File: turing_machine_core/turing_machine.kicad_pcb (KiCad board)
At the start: 2 copper layers, 165.1 x 110.5 mm, 57 parts, among them J1 External Interface, U1 74LS04, U10 AS6C1008, U11 74LS193, U12 74LS374, U13 74LS74, U14 74LS245, U15 74LS245, U16 74LS245, U17 74LS245, U18 74LS245, U19 74LS138, U2 74LS00, U20 74LS156, U3 AS6C1008, U4 74LS374, U5 74LS193, U6 74LS30, U7 AS6C1008, U8 74LS193, U9 74LS193

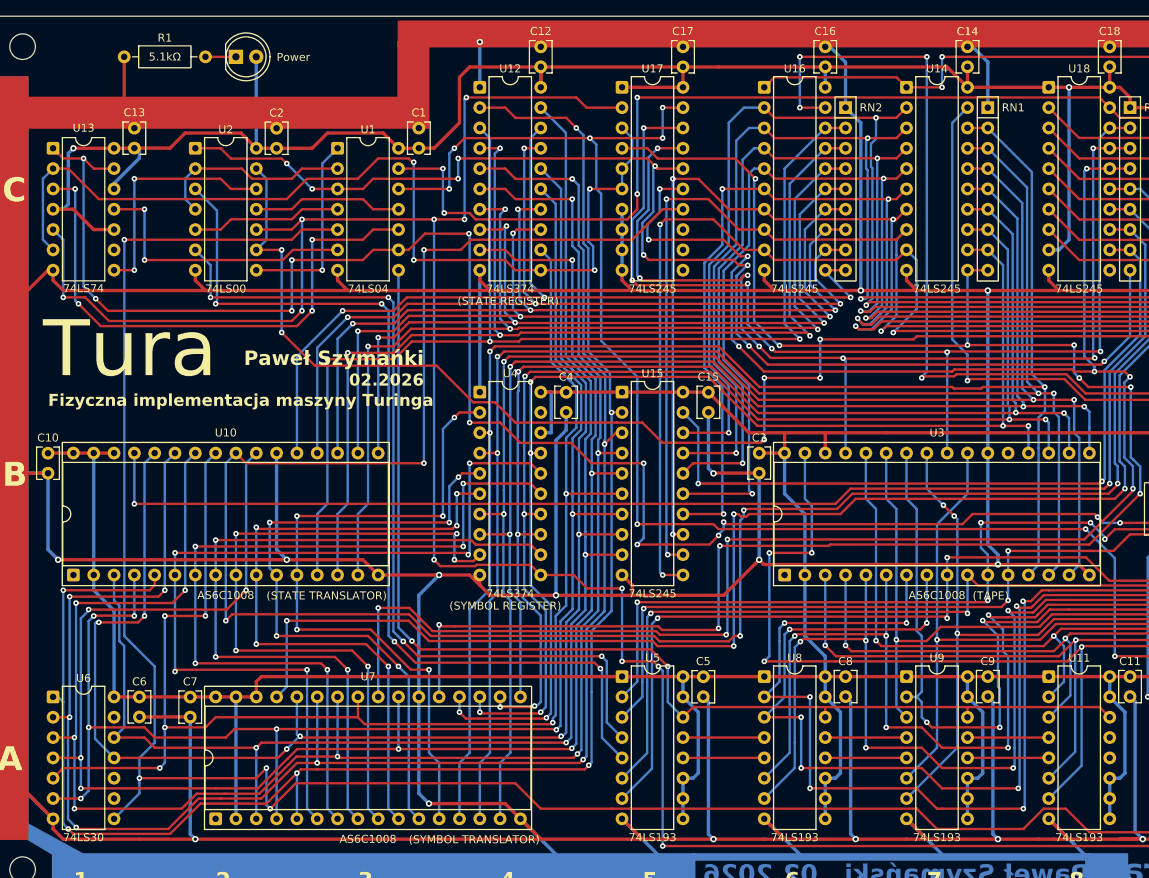
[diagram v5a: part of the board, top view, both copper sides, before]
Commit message: small cosmetic PCB changes
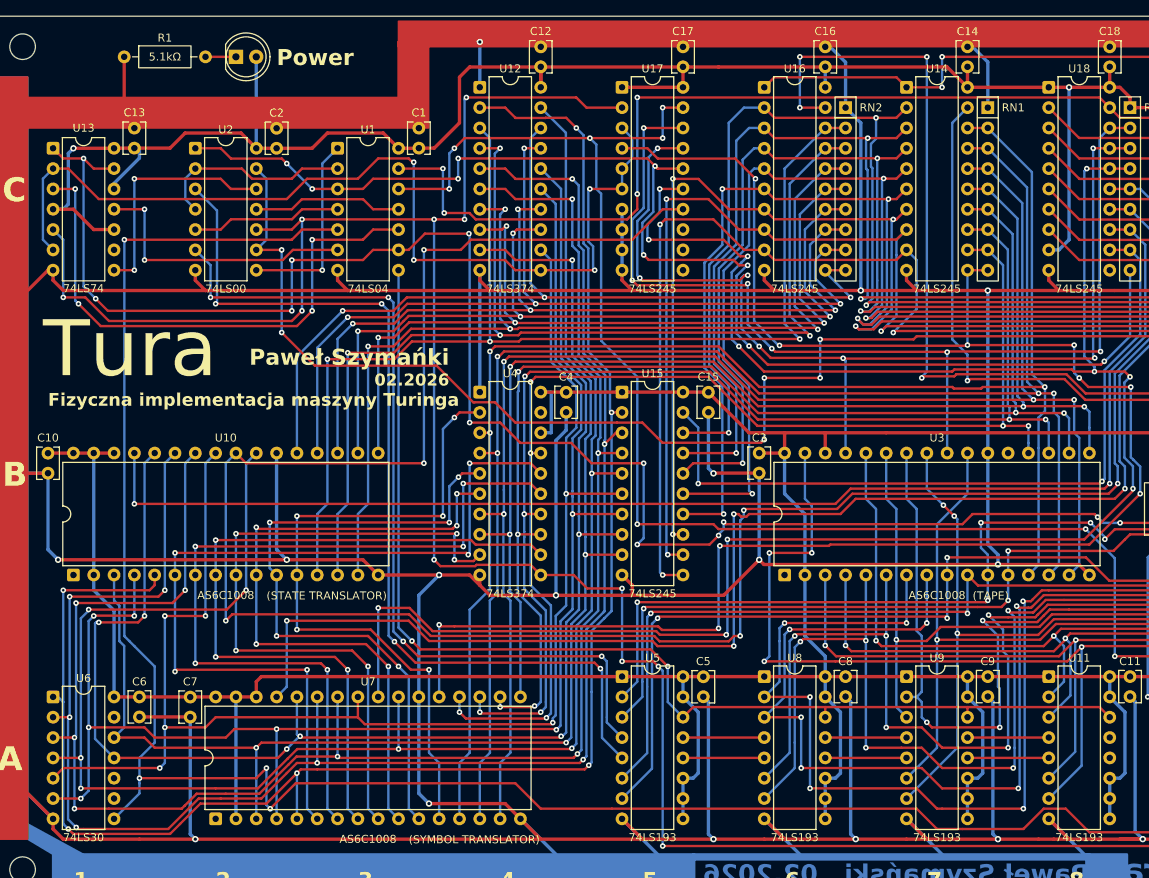
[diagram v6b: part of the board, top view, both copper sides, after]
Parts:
- removed the REF** at (226.1, 45.1)
- removed the REF** at (226.1, 64.1)
- U10, U3, U7: footprint Package_DIP:DIP-32_W15.24mm_Socket -> Package_DIP:DIP-32_W15.24mm
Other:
- board text removed: "(STATE REGISTER)"
- board text removed: "(SYMBOL REGISTER)"

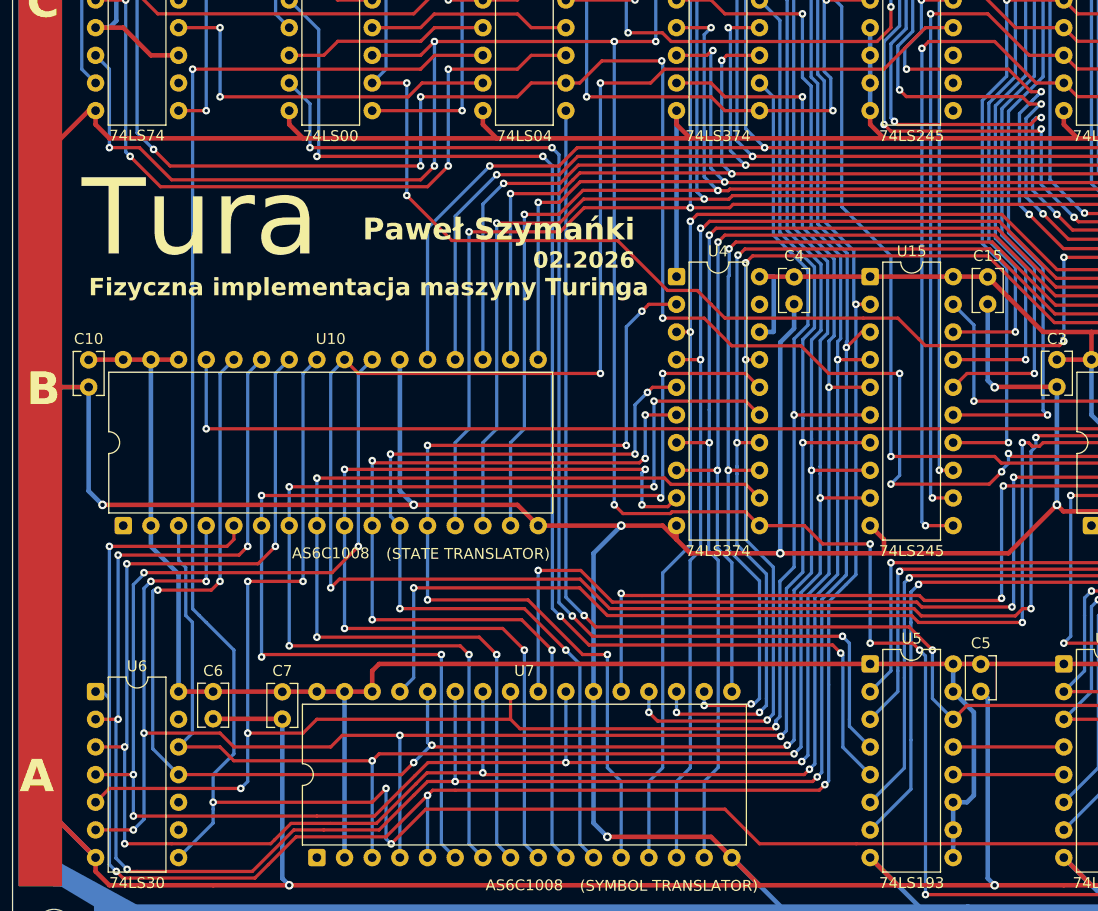
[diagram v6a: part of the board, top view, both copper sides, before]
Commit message: added two connectors to schematics and PCB design and reformatted slightly documentation
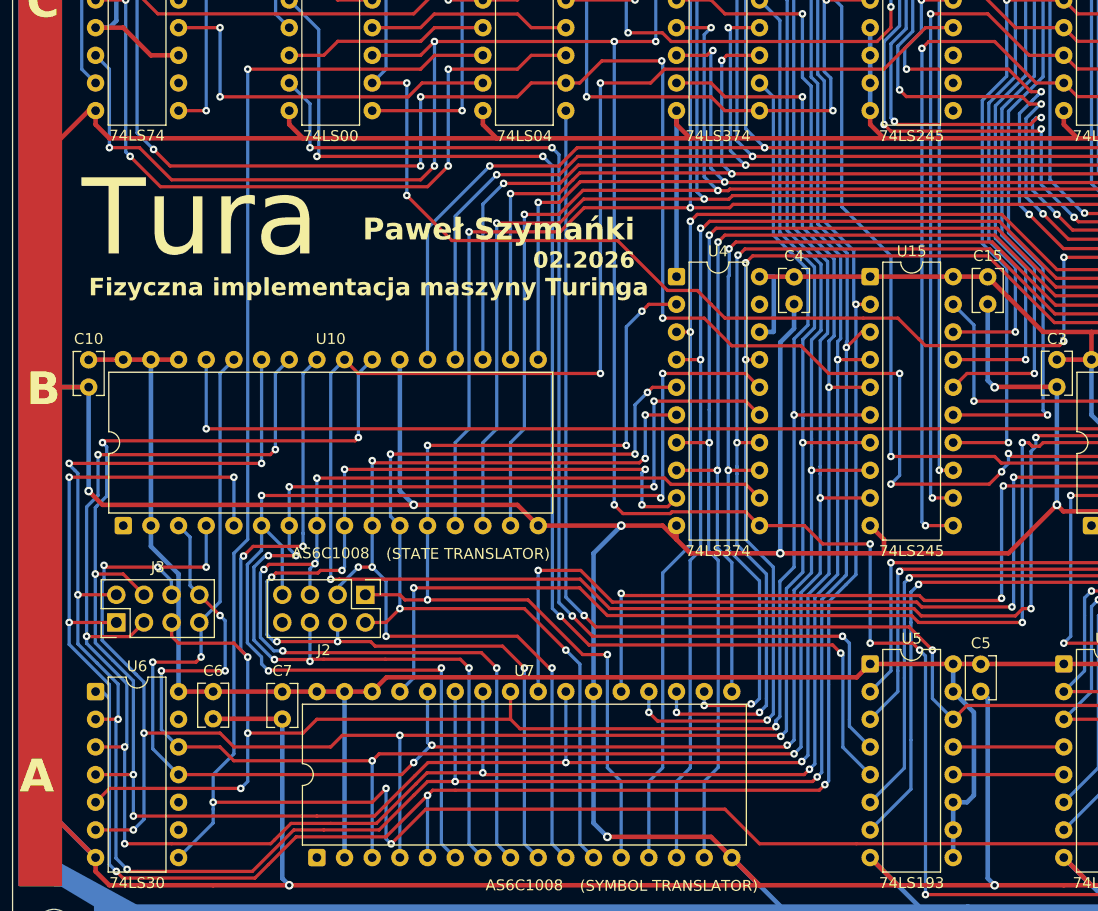
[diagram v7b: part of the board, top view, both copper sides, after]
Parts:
- added J2: Symbol Register Value Output, Connector_PinHeader_2.54mm:PinHeader_2x04_P2.54mm_Vertical, F.Cu at (57.8, 92.7)
- added J3: State Register Value Output, Connector_PinHeader_2.54mm:PinHeader_2x04_P2.54mm_Vertical, F.Cu at (34.9, 95.2)
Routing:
- net QR_{0}: track 216.3 -> 235.1 mm, vias 6 -> 8
- net SR_{3}: track 86.1 -> 100.7 mm, vias 5 -> 8
- net SR_{4}: track 92.3 -> 104.4 mm, vias 3 -> 5
- net QR_{3}: track 213.9 -> 225.7 mm, vias 8 -> 9
- net QR_{1}: track 227.0 -> 238.1 mm, vias 8 -> 9
- net QR_{2}: track 220.8 -> 231.9 mm, vias 8 -> 9
- net SR_{5}: track 102.2 -> 111.7 mm, vias 5 -> 8
- net QR_{4}: track 180.3 -> 189.5 mm, vias 6 -> 7
- net QR_{5}: track 185.1 -> 194.1 mm, vias 7 -> 8
- net SR_{6}: track 108.3 -> 116.2 mm
- net QR_{7}: track 175.6 -> 182.8 mm, vias 3 -> 6
- net ~{FINISH_STATE}: track 321.8 -> 315.7 mm
- net SR_{0}: track 86.5 -> 92.5 mm
- net SR_{2}: track 84.0 -> 87.8 mm, vias 5 -> 7
- net SR_{1}: track 82.9 -> 86.6 mm
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
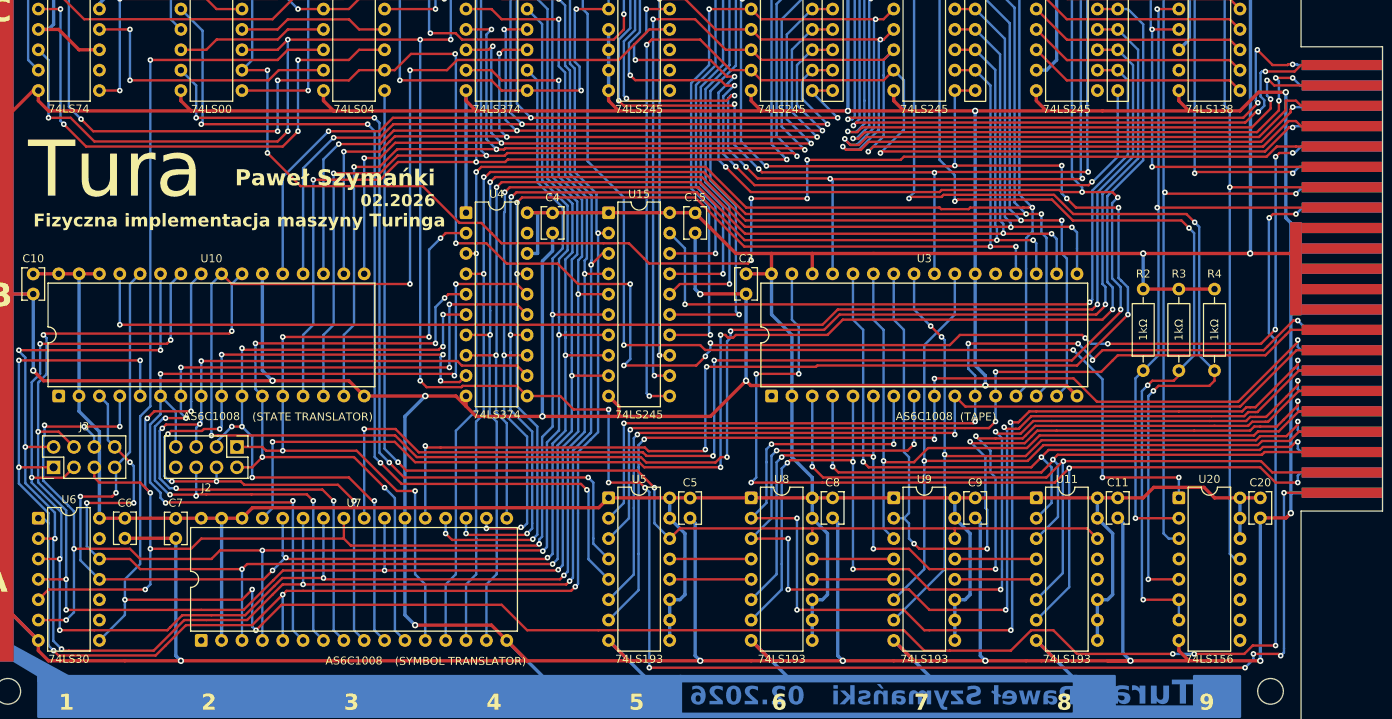
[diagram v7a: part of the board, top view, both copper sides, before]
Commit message: moved Header Position output from main connector to dedicated one and updated documentation for that
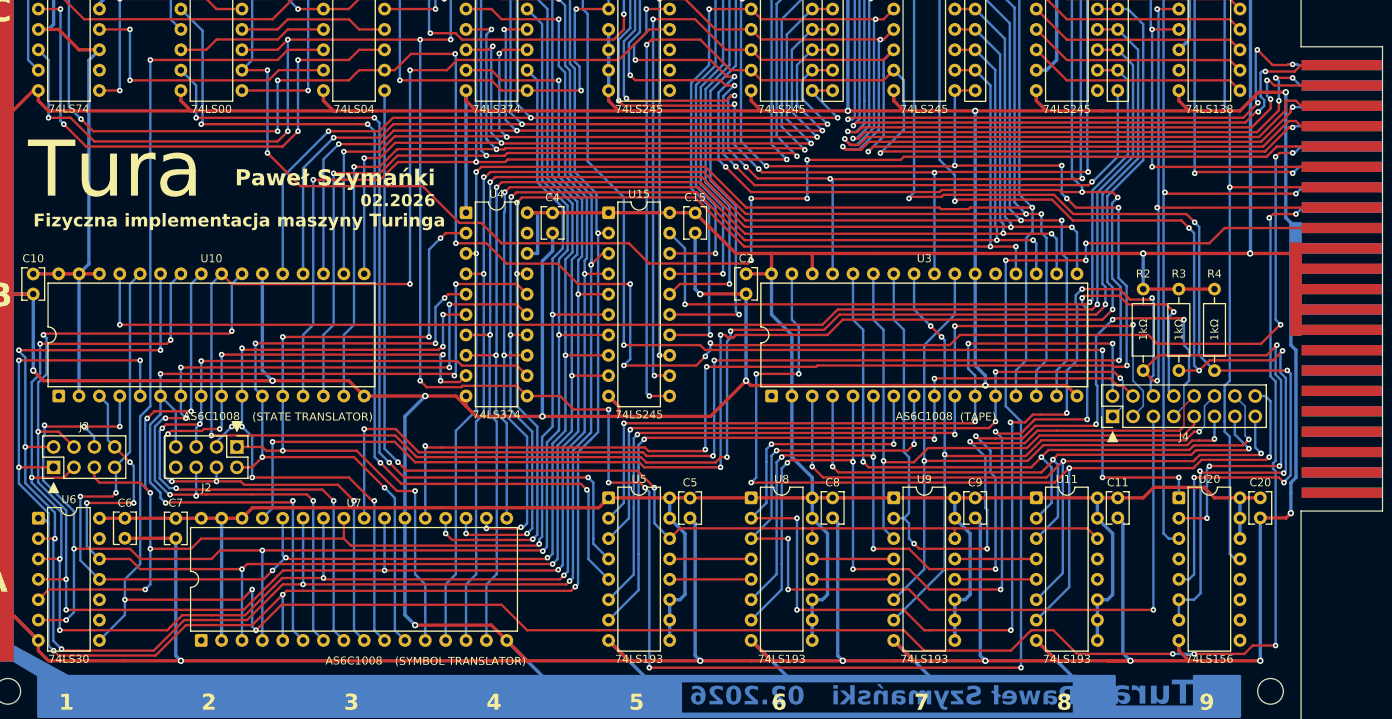
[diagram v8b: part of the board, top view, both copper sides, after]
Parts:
- added J4: Header Position Value Output, Connector_PinHeader_2.54mm:PinHeader_2x08_P2.54mm_Vertical, F.Cu at (167.0, 88.9)
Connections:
- J1 pad 17: +5V -> HP_EN
- J1 pad 27: H_{0} -> +5V
- J1 pad 28: H_{1} -> GND
- J1 pad 29: H_{2} -> unconnected-(J1-Pin_29-Pad29)
- J1 pad 30: H_{3} -> unconnected-(J1-Pin_30-Pad30)
- J1 pad 31: H_{4} -> unconnected-(J1-Pin_31-Pad31)
- J1 pad 32: H_{5} -> unconnected-(J1-Pin_32-Pad32)
- J1 pad 33: H_{6} -> unconnected-(J1-Pin_33-Pad33)
- J1 pad 34: H_{7} -> unconnected-(J1-Pin_34-Pad34)
- J1 pad 35: H_{8} -> unconnected-(J1-Pin_35-Pad35)
- J1 pad 36: H_{9} -> unconnected-(J1-Pin_36-Pad36)
- J1 pad 37: H_{10} -> unconnected-(J1-Pin_37-Pad37)
- J1 pad 38: H_{11} -> unconnected-(J1-Pin_38-Pad38)
- J1 pad 39: H_{12} -> unconnected-(J1-Pin_39-Pad39)
- J1 pad 40: H_{13} -> unconnected-(J1-Pin_40-Pad40)
- J1 pad 41: H_{14} -> unconnected-(J1-Pin_41-Pad41)
- J1 pad 42: H_{15} -> unconnected-(J1-Pin_42-Pad42)
- J1 pad 43: HP_EN -> unconnected-(J1-Pin_43-Pad43)
- J1 pad 44: GND -> unconnected-(J1-Pin_44-Pad44)
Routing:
- net HP_EN: track 325.8 -> 360.9 mm
- net ~{DT}: track 96.1 -> 127.0 mm, vias 3 -> 7
- net H_{3}: track 124.7 -> 94.0 mm, vias 4 -> 3
- net H_{4}: track 143.1 -> 117.5 mm, vias 6 -> 5
- net H_{1}: track 116.7 -> 91.2 mm, vias 6 -> 4
- net H_{0}: track 112.2 -> 88.2 mm, vias 3 -> 4
- net ~{SYMB_BUF}: track 124.4 -> 145.9 mm, vias 4 -> 6
- net H_{9}: track 110.2 -> 92.1 mm, vias 4 -> 3
- net H_{8}: track 93.9 -> 75.9 mm
- net H_{11}: track 100.2 -> 85.7 mm
- net H_{10}: track 97.4 -> 83.9 mm, vias 1 -> 2
- net +5V: track 747.9 -> 760.6 mm
- net ~{STAT_BUF}: track 159.6 -> 171.9 mm, vias 7 -> 8
- net H_{2}: track 118.4 -> 110.1 mm, vias 2 -> 4
- net H_{12}: track 85.0 -> 78.3 mm, vias 2 -> 3
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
